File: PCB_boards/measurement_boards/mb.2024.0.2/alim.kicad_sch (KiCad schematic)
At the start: 3 parts

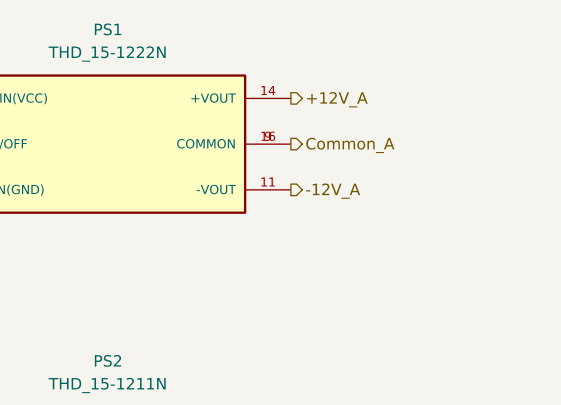
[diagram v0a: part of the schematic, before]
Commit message: correction DPS, add dischage resistor, remove 63 warning on the schemtic, remove 7 errors in schematics change resistor designation, update pcb
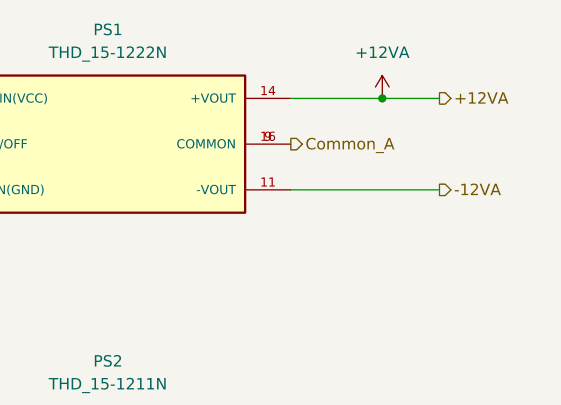
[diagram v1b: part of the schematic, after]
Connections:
- net +12V_A renamed +12VA
- net -12V_A renamed -12VA
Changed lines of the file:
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@@
     (title "Alimentations ")
+  )
+  (junction (at 137.16 40.64) (diameter 0) (color 0 0 0 0)
   )
   (no_connect (at 81.28 87.63))
@@
     (stroke (width 0) (type default))
   )
+  (wire (pts (xy 137.16 40.64) (xy 143.51 40.64))
+    (stroke (width 0) (type default))
+  )
   (wire (pts (xy 81.28 119.38) (xy 81.28 121.92))
     (stroke (width 0) (type default))
   )
+  (wire (pts (xy 127 50.8) (xy 143.51 50.8))
+    (stroke (width 0) (type default))
+  )
   (wire (pts (xy 132.08 116.84) (xy 132.08 119.38))
+    (stroke (width 0) (type default))
+  )
+  (wire (pts (xy 127 40.64) (xy 137.16 40.64))
     (stroke (width 0) (type default))
   )
@@
     (effects (font (size 1.27 1.27)) (justify left))
   )
-  (hierarchical_label "-12V_A" (shape output) (at 127 50.8 0) (fields_autoplaced)
+  (hierarchical_label "-12VA" (shape output) (at 143.51 50.8 0) (fields_autoplaced)
     (effects (font (size 1.27 1.27)) (justify left))
   )
@@
     (effects (font (size 1.27 1.27)) (justify left))
   )
-  (hierarchical_label "+12V_A" (shape output) (at 127 40.64 0) (fields_autoplaced)
+  (hierarchical_label "+12VA" (shape output) (at 143.51 40.64 0) (fields_autoplaced)
     (effects (font (size 1.27 1.27)) (justify left))
   )
@@
         )
       )
+    )
+  )
+  (symbol (lib_id "power:+12VA") (at 137.16 40.64 0) (unit 1)
+    (in_bom yes) (on_board yes) (dnp no) (fields_autoplaced)
+    (property "Reference" "#PWR04" (at 137.16 44.45 0)
+      (effects (font (size 1.27 1.27)) hide)
+    )
+    (property "Value" "+12VA" (at 137.16 35.56 0)
+      (effects (font (size 1.27 1.27)))
+    )
+    (property "Footprint" "" (at 137.16 40.64 0)
+      (effects (font (size 1.27 1.27)) hide)
+    )
+    (property "Datasheet" "" (at 137.16 40.64 0)
+      (effects (font (size 1.27 1.27)) hide)
+    )
+    (pin "1")
+    (instances
+      (project "mb.2024.0.2"
+        (path "/62d2b953-c7cc-4d07-805d-38225011d95a/9f60bb1d-ca92-41d5-b592-f34396aa7479"
+          (reference "#PWR04") (unit 1)
+        )
+      )

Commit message: update measurement board
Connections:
- net +12VA renamed +12V_A
- net -12VA renamed -12V_A
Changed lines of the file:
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@@
     (title "Alimentations ")
-  )
-  (junction (at 137.16 40.64) (diameter 0) (color 0 0 0 0)
   )
   (no_connect (at 81.28 87.63))
@@
     (stroke (width 0) (type default))
   )
-  (wire (pts (xy 137.16 40.64) (xy 143.51 40.64))
-    (stroke (width 0) (type default))
-  )
   (wire (pts (xy 81.28 119.38) (xy 81.28 121.92))
     (stroke (width 0) (type default))
   )
-  (wire (pts (xy 127 50.8) (xy 143.51 50.8))
-    (stroke (width 0) (type default))
-  )
   (wire (pts (xy 132.08 116.84) (xy 132.08 119.38))
-    (stroke (width 0) (type default))
-  )
-  (wire (pts (xy 127 40.64) (xy 137.16 40.64))
     (stroke (width 0) (type default))
   )
@@
     (effects (font (size 1.27 1.27)) (justify left))
   )
-  (hierarchical_label "-12VA" (shape output) (at 143.51 50.8 0) (fields_autoplaced)
+  (hierarchical_label "-12V_A" (shape output) (at 127 50.8 0) (fields_autoplaced)
     (effects (font (size 1.27 1.27)) (justify left))
   )
@@
     (effects (font (size 1.27 1.27)) (justify left))
   )
-  (hierarchical_label "+12VA" (shape output) (at 143.51 40.64 0) (fields_autoplaced)
+  (hierarchical_label "+12V_A" (shape output) (at 127 40.64 0) (fields_autoplaced)
     (effects (font (size 1.27 1.27)) (justify left))
   )
@@
         )
       )
-    )
-  )
-  (symbol (lib_id "power:+12VA") (at 137.16 40.64 0) (unit 1)
-    (in_bom yes) (on_board yes) (dnp no) (fields_autoplaced)
-    (property "Reference" "#PWR04" (at 137.16 44.45 0)
-      (effects (font (size 1.27 1.27)) hide)
-    )
-    (property "Value" "+12VA" (at 137.16 35.56 0)
-      (effects (font (size 1.27 1.27)))
-    )
-    (property "Footprint" "" (at 137.16 40.64 0)
-      (effects (font (size 1.27 1.27)) hide)
-    )
-    (property "Datasheet" "" (at 137.16 40.64 0)
-      (effects (font (size 1.27 1.27)) hide)
-    )
-    (pin "1")
-    (instances
-      (project "mb.2024.0.2"
-        (path "/62d2b953-c7cc-4d07-805d-38225011d95a/9f60bb1d-ca92-41d5-b592-f34396aa7479"
-          (reference "#PWR04") (unit 1)
-        )
-      )
